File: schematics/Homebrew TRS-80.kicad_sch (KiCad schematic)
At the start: 66 parts, among them J3 Keyboard Header, J4 Keyboard Header, U1 TMPZ84C00A, U10 74LS32, U11 74LS74, U12 74LS74, U13 74LS367, U14 74LS367, U15 MK4164N, U16 MK4164N, U17 MK4164N, U18 MK4164N, U19 MK4164N, U2 74LS367, U20 MK4164N, U21 MK4164N, U22 MK4164N, U23 MK4164N, U24 MK4164N, U25 MK4164N, U26 MK4164N, U27 MK4164N, U28 MK4164N, U29 MK4164N, U3 74LS367, U30 MK4164N, U31 74LS157, U32 74LS157, U33 2732, U34 2732, U35 2732, U36 74LS132, U37 74LS02, U38 74LS04, U39 74LS92, U4 74LS367, U40 74LS368, U42 74LS05, U43 74LS05, U44 74LS05, U45 74LS05, U46 74LS05, U47 74LS05, U48 74LS368, U5 74LS367, U6 74LS367, U7 74LS367, U8 74LS367, U9 74LS367, Y1 ASDMB-xxxMHz

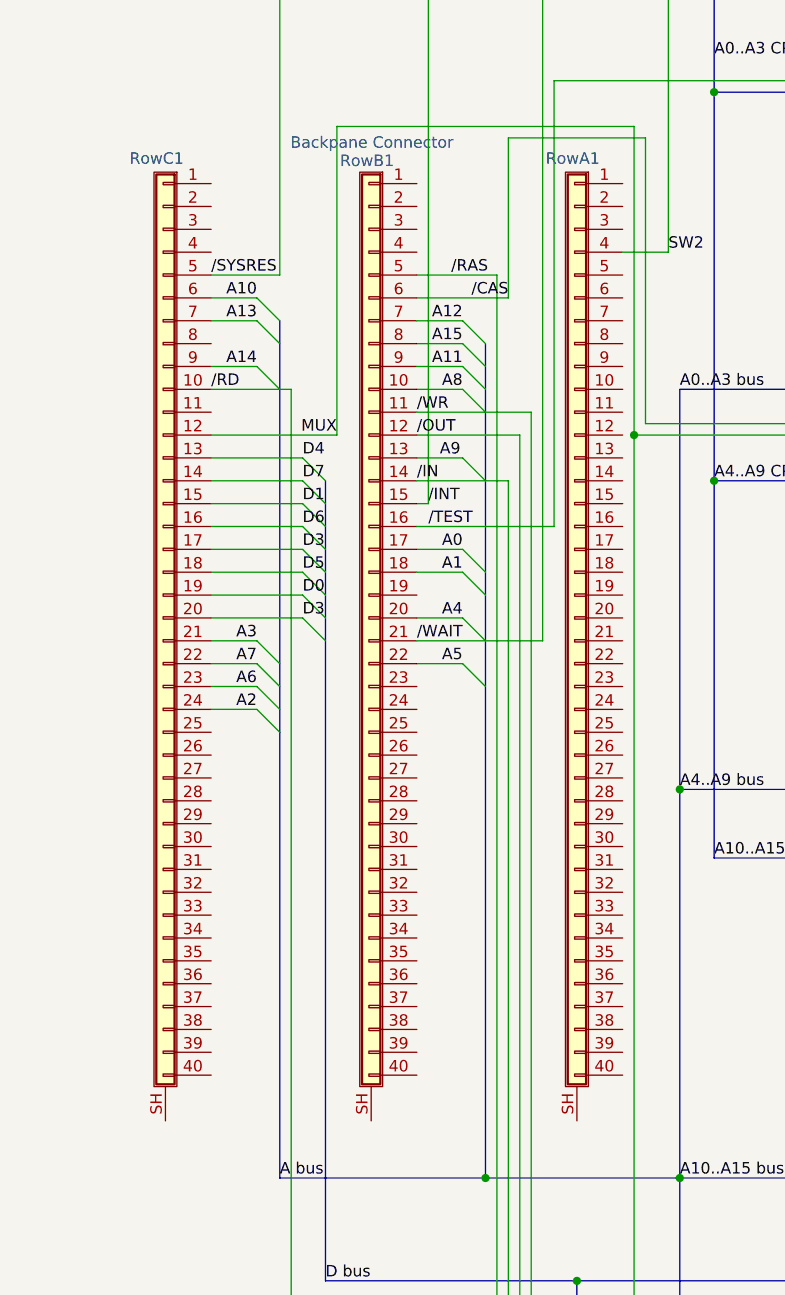
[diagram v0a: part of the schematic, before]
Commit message: updated schematics, added video resources
updated schematics, added video resources
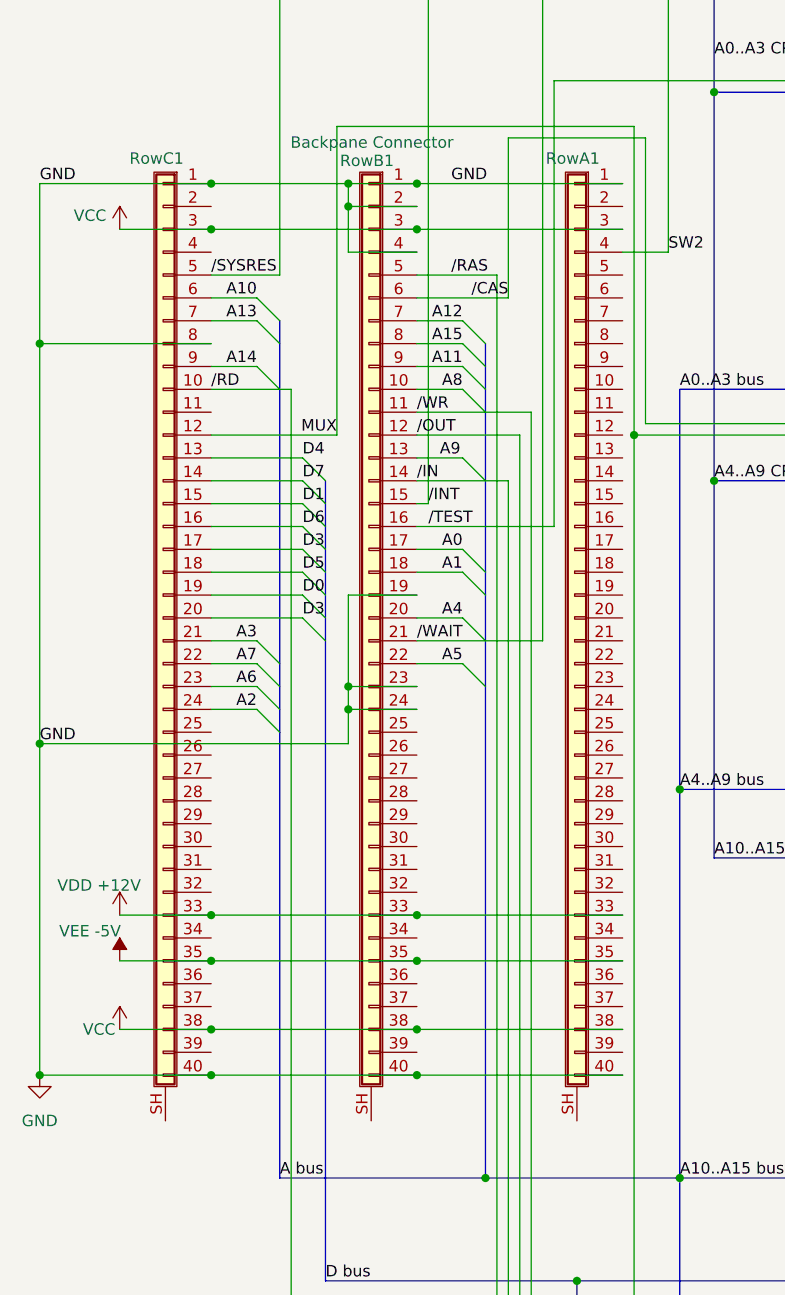
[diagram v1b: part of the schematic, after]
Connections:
- net GND: now also RowA1.1 (Pin_1), RowA1.40 (Pin_40), RowB1.1 (Pin_1), RowB1.19 (Pin_19), RowB1.2 (Pin_2), RowB1.23 (Pin_23), RowB1.24 (Pin_24), RowB1.4 (Pin_4), RowB1.40 (Pin_40), RowC1.1 (Pin_1), RowC1.40 (Pin_40), RowC1.8 (Pin_8)
- net VCC: now also RowA1.3 (Pin_3), RowA1.38 (Pin_38), RowB1.3 (Pin_3), RowB1.38 (Pin_38), RowC1.3 (Pin_3), RowC1.38 (Pin_38)
- net VDD +12V: now reaches RowB1.33 (Pin_33)
- net VDD +12V: now also RowA1.33 (Pin_33), RowC1.33 (Pin_33)
- net VEE -5V: now reaches RowB1.35 (Pin_35)
- net VEE -5V: now also RowA1.35 (Pin_35), RowC1.35 (Pin_35)

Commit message: updated schematics and added pictures
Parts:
- U16, U17, U18, U19, U20, U21, U22, U23, U24, U25, U26, U27, U28, U29, U30: value MK4164N -> uPD416c; symbol Memory_RAM:MK4164N -> uPD416c:uPD416c
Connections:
- net /INTAK? is gone; now on net /INTAK: U37.10
- net D2: now also RowC1.20 (Pin_20)
- net D3: no longer RowC1.20 (Pin_20)
- net VCC: no longer U15.9 (A7), U16.8 (VCC), U17.8 (VCC), U18.8 (VCC), U19.8 (VCC), U20.8 (VCC), U21.8 (VCC), U22.8 (VCC), U23.8 (VCC), U24.8 (VCC), U25.8 (VCC), U26.8 (VCC), U27.8 (VCC), U28.8 (VCC), U29.8 (VCC), U30.8 (VCC)
- net /TEST: now also U38.3
- net VEE: now reaches U16.1 (VBB), U17.1 (VBB), U18.1 (VBB), U19.1 (VBB), U20.1 (VBB), U21.1 (VBB), U22.1 (VBB), U23.1 (VBB), U24.1 (VBB), U25.1 (VBB), U26.1 (VBB), U27.1 (VBB), U28.1 (VBB), U29.1 (VBB), U30.1 (VBB)
- net VEE: no longer C1.1, U15.1 (~{RFSH})
- net /INTAK: now reaches U38.1
- net INTAK: now reaches U38.2
- net INTAK: now also RowC1.11 (Pin_11)
- net /ENABLE: now reaches U2.1 (OEa), U2.15 (OEb), U5.1 (OEa), U5.15 (OEb), U6.1 (OEa), U6.15 (OEb), U9.1 (OEa), U9.15 (OEb)
- net /ENABLE: now also U38.4
- new net: C1.1, U15.1 (~{RFSH})
- new net VDD: U16.8 (VDD), U17.8 (VDD), U18.8 (VDD), U19.8 (VDD), U20.8 (VDD), U21.8 (VDD), U22.8 (VDD), U23.8 (VDD), U24.8 (VDD), U25.8 (VDD), U26.8 (VDD), U27.8 (VDD), U28.8 (VDD), U29.8 (VDD), U30.8 (VDD)
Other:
- moved on the sheet: U38A, U38B

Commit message: updated schematics
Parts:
- added C5, C7: 104, symbol Device:C
- added C6: ???, symbol Device:C
- C1: value 104 -> 2.2uF
- U15: symbol Memory_RAM:MK4164N -> uPD416c:uPD416c
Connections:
- net GND: now also C5.2, C6.2, C7.2
- net MD0: now also U13.3 (O1a), U15.14 (DOUT), U15.2 (DIN), U17.14 (DOUT), U17.2 (DIN); no longer U14.10 (I4), U14.9 (O4a), U28.2 (DIN), U30.2 (DIN)
- net MD1: now also U13.4 (I2), U13.5 (O2a), U19.14 (DOUT), U19.2 (DIN), U21.14 (DOUT), U21.2 (DIN); no longer U14.2 (I1), U14.3 (O1a), U16.14 (DOUT), U16.2 (DIN), U18.14 (DOUT), U18.2 (DIN)
- net MD2: now also U13.7 (O3a), U23.14 (DOUT), U23.2 (DIN), U25.14 (DOUT), U25.2 (DIN); no longer U14.4 (I2), U14.5 (O2a), U20.14 (DOUT), U20.2 (DIN), U22.14 (DOUT), U22.2 (DIN)
- net MD3: now also U13.10 (I4), U13.9 (O4a), U27.14 (DOUT), U27.2 (DIN), U29.14 (DOUT), U29.2 (DIN); no longer U14.6 (I3), U14.7 (O3a), U24.14 (DOUT), U24.2 (DIN), U26.14 (DOUT), U26.2 (DIN)
- net MD4: now also U14.2 (I1), U14.3 (O1a), U16.14 (DOUT), U16.2 (DIN), U18.14 (DOUT), U18.2 (DIN); no longer U13.10 (I4), U13.9 (O4a), U27.14 (DOUT), U27.2 (DIN), U29.2 (DIN)
- net MD5: now also U14.4 (I2), U14.5 (O2a), U20.14 (DOUT), U20.2 (DIN), U22.14 (DOUT), U22.2 (DIN); no longer U13.3 (O1a), U15.14 (DOUT), U15.2 (DIN), U17.14 (DOUT), U17.2 (DIN)
- net MD6: now also U14.6 (I3), U14.7 (O3a), U24.14 (DOUT), U24.2 (DIN), U26.14 (DOUT), U26.2 (DIN); no longer U13.4 (I2), U13.5 (O2a), U19.14 (DOUT), U19.2 (DIN), U21.14 (DOUT), U21.2 (DIN)
- net MD7: now also U14.10 (I4), U14.9 (O4a), U28.14 (DOUT), U28.2 (DIN), U30.14 (DOUT), U30.2 (DIN); no longer U13.7 (O3a), U23.14 (DOUT), U23.2 (DIN), U25.14 (DOUT), U25.2 (DIN)
- net VCC: now also U15.9 (VCC); no longer U15.8 (VCC)
- net VDD: now also U15.8 (VDD), C5.1, C6.1
- net VEE: now also C1.1, U15.1 (VBB), C7.1
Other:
- moved on the sheet: C1, U14
